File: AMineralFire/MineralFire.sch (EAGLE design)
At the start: 27 parts, among them Q1 20MHz, U1 328P, U3 7805

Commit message: First Attempt at layout
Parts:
- added +5V, GND, LED-TX: WIREPAD4,16O1,6, wirepad:WIREPAD4,16O1,6
- added C3: 100pF, SparkFun-Capacitors:100PF-0603-50V-5%
- added D3: 200mA/100V/1V, SparkFun-DiscreteSemi:DIODE-1N4148
- added D4: Gate LED, SparkFun-LED:LED3MM
- added GATE1, TRIGATEIN: S_JACK, INSTRUO:S_JACK
- added IC1: OP-AMP, SparkFun-IC-Amplifiers:OPAMP-DUALU
- added MODESW3: TOGGLE_ON_OFF_ON, INSTRUO:TOGGLE_ON_OFF_ON
- added R13: 1M, SparkFun-Resistors:1MOHM-HORIZ-1/4W-5%
- added R15: 330, SparkFun-Resistors:330OHM-HORIZ-1/10W-5%
- added R16, R17, R19, R5, R6, R8: 100k, SparkFun-Resistors:100KOHM-HORIZ-1/4W-5%
- added R18, R4: 1k, SparkFun-Resistors:1KOHM-HORIZ-1/4W-5%
- added R7: 10k, SparkFun-Resistors:10KOHM-HORIZ-1/4W-5%
- added T1: 200mA/40V, SparkFun-DiscreteSemi:TRANS_NPN-2N3904
- C1, C2: value 22p -> 22pF; device rcl:C-USC0805K -> SparkFun-Capacitors:22PF-PTH-2.54MM-200V-5%
- C10, C11, C12, C8, C9: value 0.1u -> 0.1uF; device rcl:C-USC0805K -> SparkFun-Capacitors:0.1UF-KIT-EZ-50V-20%
- C4, C5, C7: value 10u -> 10uF; device rcl:CPOL-US153CLV-0505 -> SparkFun-Capacitors:10UF-POLAR-RADIAL-2.5MM-25V-20%
- D1, D2: value (none) -> 200mA/100V/1V; device adafruit:DIODESMA -> SparkFun-DiscreteSemi:DIODE-1N4148
- R1, R10: value 1K -> 1k; device rcl:R-US_R0805 -> SparkFun-Resistors:1KOHM-HORIZ-1/4W-5%
- R11, R12, R2, R3: value 100K -> 100k; device rcl:R-US_R0805 -> SparkFun-Resistors:100KOHM-HORIZ-1/4W-5%
- U3: device INSTRUO:V-REG -> SparkFun-IC-Power:R-78E5.0-1.0
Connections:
- new net N$15: R13.2, R8.1, T1.B
- new net N$18: R8.2, TRIGATEIN.TIP
- new net N$31: D4.C, R15.1
- new net N$32: C3.1, IC1G1.-IN, R16.1, R17.2
- new net N$33: C3.2, IC1G1.OUT, R18.1
- new net N$34: D3.A, R16.2, R18.2
- new net N$4: MODESW3.P, R4.1
- new net N$5: LED-TX.P, U1.PB1(OC1A)
- new net N$74: D3.C, GATE1.TIP
- new net T5: MODESW3.S, R5.2, U1.PD0(RXD)
- new net T6: MODESW3.O, R6.2, U1.PD1(TXD)
- new net TRIGO: D4.A, IC1G1.+IN, R19.2, U1.PB0(ICP)
- net +5V: now also +5V.P, R5.1, R6.1, R7.2
- net GND: now also GATE1.GND, GND.P, R13.1, R15.2, R17.1, R19.1, R4.2, T1.E, TRIGATEIN.GND
- net TRIG: now also R7.1, T1.C
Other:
- moved on the sheet: C1, C10, C11, C12, C2, C8, C9, U3

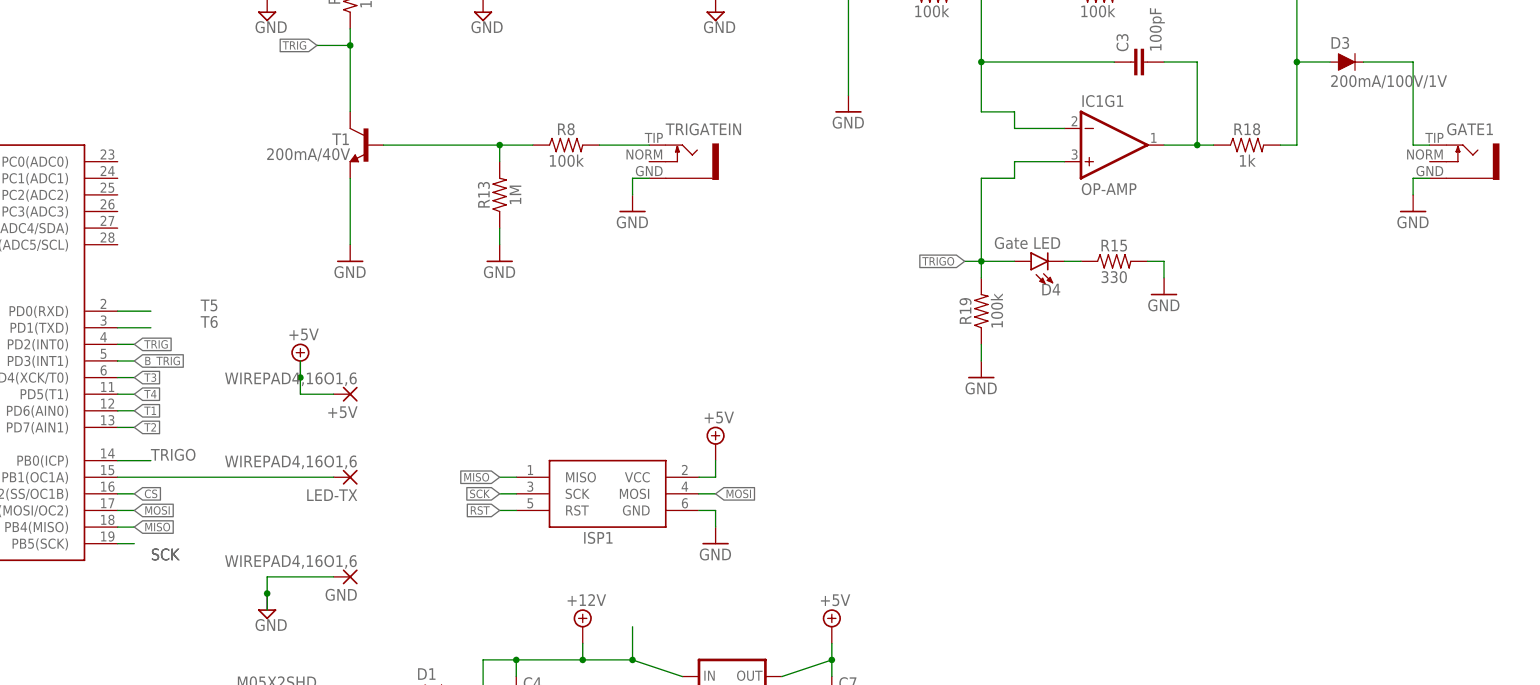
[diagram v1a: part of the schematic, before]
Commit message: ground in fill
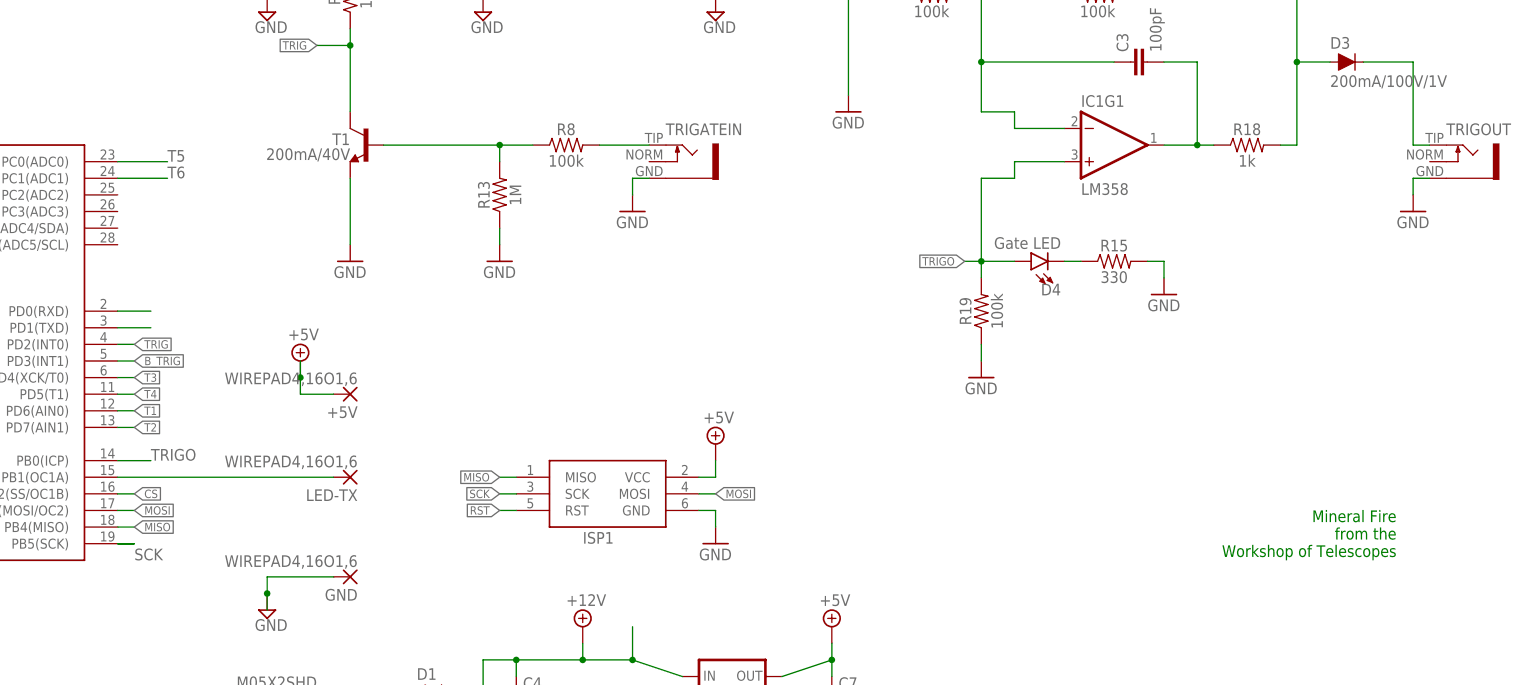
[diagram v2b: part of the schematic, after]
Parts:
- IC1: value OP-AMP -> LM358; device SparkFun-IC-Amplifiers:OPAMP-DUALU -> SparkFun-IC-Amplifiers:LM358
- Q1: device adafruit:CRYSTALHC49UP -> adafruit:CRYSTALHC49U70
- renumbered GATE1 to TRIGOUT
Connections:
- net T5: now also U1.PC0(ADC0)
- net T6: now also U1.PC1(ADC1)
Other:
- note added: "Mineral Fire from the Workshop of Telescopes"

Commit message: New Layout
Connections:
- net +12V: now also IC1G3.P$V+
- net GND: now also IC1G3.P$V-
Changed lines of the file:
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@@
 <grid distance="0.1" unitdist="inch" unit="inch" style="lines" multiple="1" display="no" altdistance="0.01" altunitdist="inch" altunit="inch"/>
 <layers>
-<layer number="1" name="Top" color="4" fill="1" visible="yes" active="no"/>
-<layer number="2" name="Route2" color="1" fill="3" visible="yes" active="no"/>
-<layer number="3" name="Route3" color="4" fill="3" visible="yes" active="no"/>
-<layer number="4" name="Route4" color="1" fill="4" visible="yes" active="no"/>
-<layer number="5" name="Route5" color="4" fill="4" visible="yes" active="no"/>
-<layer number="6" name="Route6" color="1" fill="8" visible="yes" active="no"/>
-<layer number="7" name="Route7" color="4" fill="8" visible="yes" active="no"/>
-<layer number="8" name="Route8" color="1" fill="2" visible="yes" active="no"/>
-<layer number="9" name="Route9" color="4" fill="2" visible="yes" active="no"/>
-<layer number="10" name="Route10" color="1" fill="7" visible="yes" active="no"/>
-<layer number="11" name="Route11" color="4" fill="7" visible="yes" active="no"/>
-<layer number="12" name="Route12" color="1" fill="5" visible="yes" active="no"/>
-<layer number="13" name="Route13" color="4" fill="5" visible="yes" active="no"/>
-<layer number="14" name="Route14" color="1" fill="6" visible="yes" active="no"/>
-<layer number="15" name="Route15" color="4" fill="6" visible="yes" active="no"/>
-<layer number="16" name="Bottom" color="1" fill="1" visible="yes" active="no"/>
-<layer number="17" name="Pads" color="2" fill="1" visible="yes" active="no"/>
-<layer number="18" name="Vias" color="2" fill="1" visible="yes" active="no"/>
-<layer number="19" name="Unrouted" color="6" fill="1" visible="yes" active="no"/>
-<layer number="20" name="Dimension" color="15" fill="1" visible="yes" active="no"/>
-<layer number="21" name="tPlace" color="7" fill="1" visible="yes" active="no"/>
-<layer number="22" name="bPlace" color="7" fill="1" visible="yes" active="no"/>
-<layer number="23" name="tOrigins" color="15" fill="1" visible="yes" active="no"/>
-<layer number="24" name="bOrigins" color="15" fill="1" visible="yes" active="no"/>
-<layer number="25" name="tNames" color="7" fill="1" visible="yes" active="no"/>
-<layer number="26" name="bNames" color="7" fill="1" visible="yes" active="no"/>
-<layer number="27" name="tValues" color="7" fill="1" visible="yes" active="no"/>
-<layer number="28" name="bValues" color="7" fill="1" visible="yes" active="no"/>
+<layer number="1" name="Top" color="4" fill="1" visible="no" active="no"/>
+<layer number="2" name="Route2" color="1" fill="3" visible="no" active="no"/>
+<layer number="3" name="Route3" color="4" fill="3" visible="no" active="no"/>
+<layer number="4" name="Route4" color="1" fill="4" visible="no" active="no"/>
+<layer number="5" name="Route5" color="4" fill="4" visible="no" active="no"/>
+<layer number="6" name="Route6" color="1" fill="8" visible="no" active="no"/>
+<layer number="7" name="Route7" color="4" fill="8" visible="no" active="no"/>
+<layer number="8" name="Route8" color="1" fill="2" visible="no" active="no"/>
+<layer number="9" name="Route9" color="4" fill="2" visible="no" active="no"/>
+<layer number="10" name="Route10" color="1" fill="7" visible="no" active="no"/>
+<layer number="11" name="Route11" color="4" fill="7" visible="no" active="no"/>
+<layer number="12" name="Route12" color="1" fill="5" visible="no" active="no"/>
+<layer number="13" name="Route13" color="4" fill="5" visible="no" active="no"/>
+<layer number="14" name="Route14" color="1" fill="6" visible="no" active="no"/>
+<layer number="15" name="Route15" color="4" fill="6" visible="no" active="no"/>
+<layer number="16" name="Bottom" color="1" fill="1" visible="no" active="no"/>
+<layer number="17" name="Pads" color="2" fill="1" visible="no" active="no"/>
+<layer number="18" name="Vias" color="2" fill="1" visible="no" active="no"/>
+<layer number="19" name="Unrouted" color="6" fill="1" visible="no" active="no"/>
+<layer number="20" name="Dimension" color="15" fill="1" visible="no" active="no"/>
+<layer number="21" name="tPlace" color="7" fill="1" visible="no" active="no"/>
+<layer number="22" name="bPlace" color="7" fill="1" visible="no" active="no"/>
+<layer number="23" name="tOrigins" color="15" fill="1" visible="no" active="no"/>
+<layer number="24" name="bOrigins" color="15" fill="1" visible="no" active="no"/>
+<layer number="25" name="tNames" color="7" fill="1" visible="no" active="no"/>
+<layer number="26" name="bNames" color="7" fill="1" visible="no" active="no"/>
+<layer number="27" name="tValues" color="7" fill="1" visible="no" active="no"/>
+<layer number="28" name="bValues" color="7" fill="1" visible="no" active="no"/>
 <layer number="29" name="tStop" color="7" fill="3" visible="no" active="no"/>
 <layer number="30" name="bStop" color="7" fill="6" visible="no" active="no"/>
@@
 <layer number="35" name="tGlue" color="7" fill="4" visible="no" active="no"/>
 <layer number="36" name="bGlue" color="7" fill="5" visible="no" active="no"/>
-<layer number="37" name="tTest" color="7" fill="1" visible="yes" active="no"/>
-<layer number="38" name="bTest" color="7" fill="1" visible="yes" active="no"/>
+<layer number="37" name="tTest" color="7" fill="1" visible="no" active="no"/>
+<layer number="38" name="bTest" color="7" fill="1" visible="no" active="no"/>
 <layer number="39" name="tKeepout" color="4" fill="11" visible="no" active="no"/>
 <layer number="40" name="bKeepout" color="1" fill="11" visible="no" active="no"/>
@@
 <layer number="44" name="Drills" color="7" fill="1" visible="no" active="no"/>
 <layer number="45" name="Holes" color="7" fill="1" visible="no" active="no"/>
-<layer number="46" name="Milling" color="3" fill="1" visible="yes" active="no"/>
-<layer number="47" name="Measures" color="7" fill="1" visible="yes" active="no"/>
-<layer number="48" name="Document" color="7" fill="1" visible="yes" active="no"/>
-<layer number="49" name="Reference" color="7" fill="1" visible="yes" active="no"/>
-<layer number="50" name="dxf" color="7" fill="1" visible="yes" active="no"/>
-<layer number="51" name="tDocu" color="7" fill="1" visible="yes" active="no"/>
-<layer number="52" name="bDocu" color="7" fill="1" visible="yes" active="no"/>
-<layer number="53" name="tGND_GNDA" color="7" fill="9" visible="yes" active="no"/>
-<layer number="54" name="bGND_GNDA" color="1" fill="9" visible="yes" active="no"/>
-<layer number="56" name="wert" color="7" fill="1" visible="yes" active="no"/>
-<layer number="57" name="tCAD" color="7" fill="1" visible="yes" active="no"/>
-<layer number="59" name="tCarbon" color="7" fill="1" visible="yes" active="no"/>
-<layer number="60" name="bCarbon" color="7" fill="1" visible="yes" active="no"/>
+<layer number="46" name="Milling" color="3" fill="1" visible="no" active="no"/>
+<layer number="47" name="Measures" color="7" fill="1" visible="no" active="no"/>
+<layer number="48" name="Document" color="7" fill="1" visible="no" active="no"/>
+<layer number="49" name="Reference" color="7" fill="1" visible="no" active="no"/>
+<layer number="50" name="dxf" color="7" fill="1" visible="no" active="no"/>
+<layer number="51" name="tDocu" color="7" fill="1" visible="no" active="no"/>
+<layer number="52" name="bDocu" color="7" fill="1" visible="no" active="no"/>
+<layer number="53" name="tGND_GNDA" color="7" fill="9" visible="no" active="no"/>
+<layer number="54" name="bGND_GNDA" color="1" fill="9" visible="no" active="no"/>
+<layer number="56" name="wert" color="7" fill="1" visible="no" active="no"/>
+<layer number="57" name="tCAD" color="7" fill="1" visible="no" active="no"/>
+<layer number="59" name="tCarbon" color="7" fill="1" visible="no" active="no"/>
+<layer number="60" name="bCarbon" color="7" fill="1" visible="no" active="no"/>
 <layer number="90" name="Modules" color="5" fill="1" visible="yes" active="yes"/>
 <layer number="91" name="Nets" color="2" fill="1" visible="yes" active="yes"/>
@@
 <part name="+5V" library="wirepad" deviceset="WIREPAD" device="4,16O1,6"/>
 <part name="SUPPLY20" library="supply2" deviceset="+5V" device=""/>
+<part name="SUPPLY22" library="supply2" deviceset="+12V" device=""/>
+<part name="SUPPLY23" library="supply2" deviceset="GND" device=""/>
 </parts>
 <sheets>
@@
 <instance part="+5V" gate="G$1" x="147.32" y="33.02" rot="R180"/>
 <instance part="SUPPLY20" gate="+5V" x="139.7" y="38.1"/>
+<instance part="IC1" gate="G3" x="289.56" y="45.72"/>
+<instance part="SUPPLY22" gate="+12V" x="289.56" y="58.42"/>
+<instance part="SUPPLY23" gate="GND" x="289.56" y="35.56"/>
 </instances>
 <busses>
@@
 <junction x="134.62" y="2.54"/>
 </segment>
+<segment>
+<pinref part="IC1" gate="G3" pin="P$V-"/>
+<pinref part="SUPPLY23" gate="GND" pin="GND"/>
+</segment>
 </net>
 <net name="RST" class="0">
@@
 <wire x1="20.32" y1="-2.54" x2="20.32" y2="0" width="0.1524" layer="91"/>
 </segment>
-</net>
+<segment>
+<pinref part="IC1" gate="G3" pin="P$V+"/>
+<wire x1="289.56" y1="53.34" x2="289.56" y2="55.88" width="0.1524" layer="91"/>
+<pinref part="SUPPLY22" gate="+12V" pin="+12V"/>
+<wire x1="289.56" y1="55.88" x2="289.56" y2="58.42" width="0.1524" layer="91"/>
+<junction x="289.56" y="55.88"/>
+</segment>
+</net>
